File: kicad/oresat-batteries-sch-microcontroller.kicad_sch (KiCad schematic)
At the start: 31 parts, among them J4 ORESAT-DEBUG-CONNECTOR-ALL, U20 TCAN330, U21 STM32F091C, X3 ECS-160-10-36Q-ES-TR

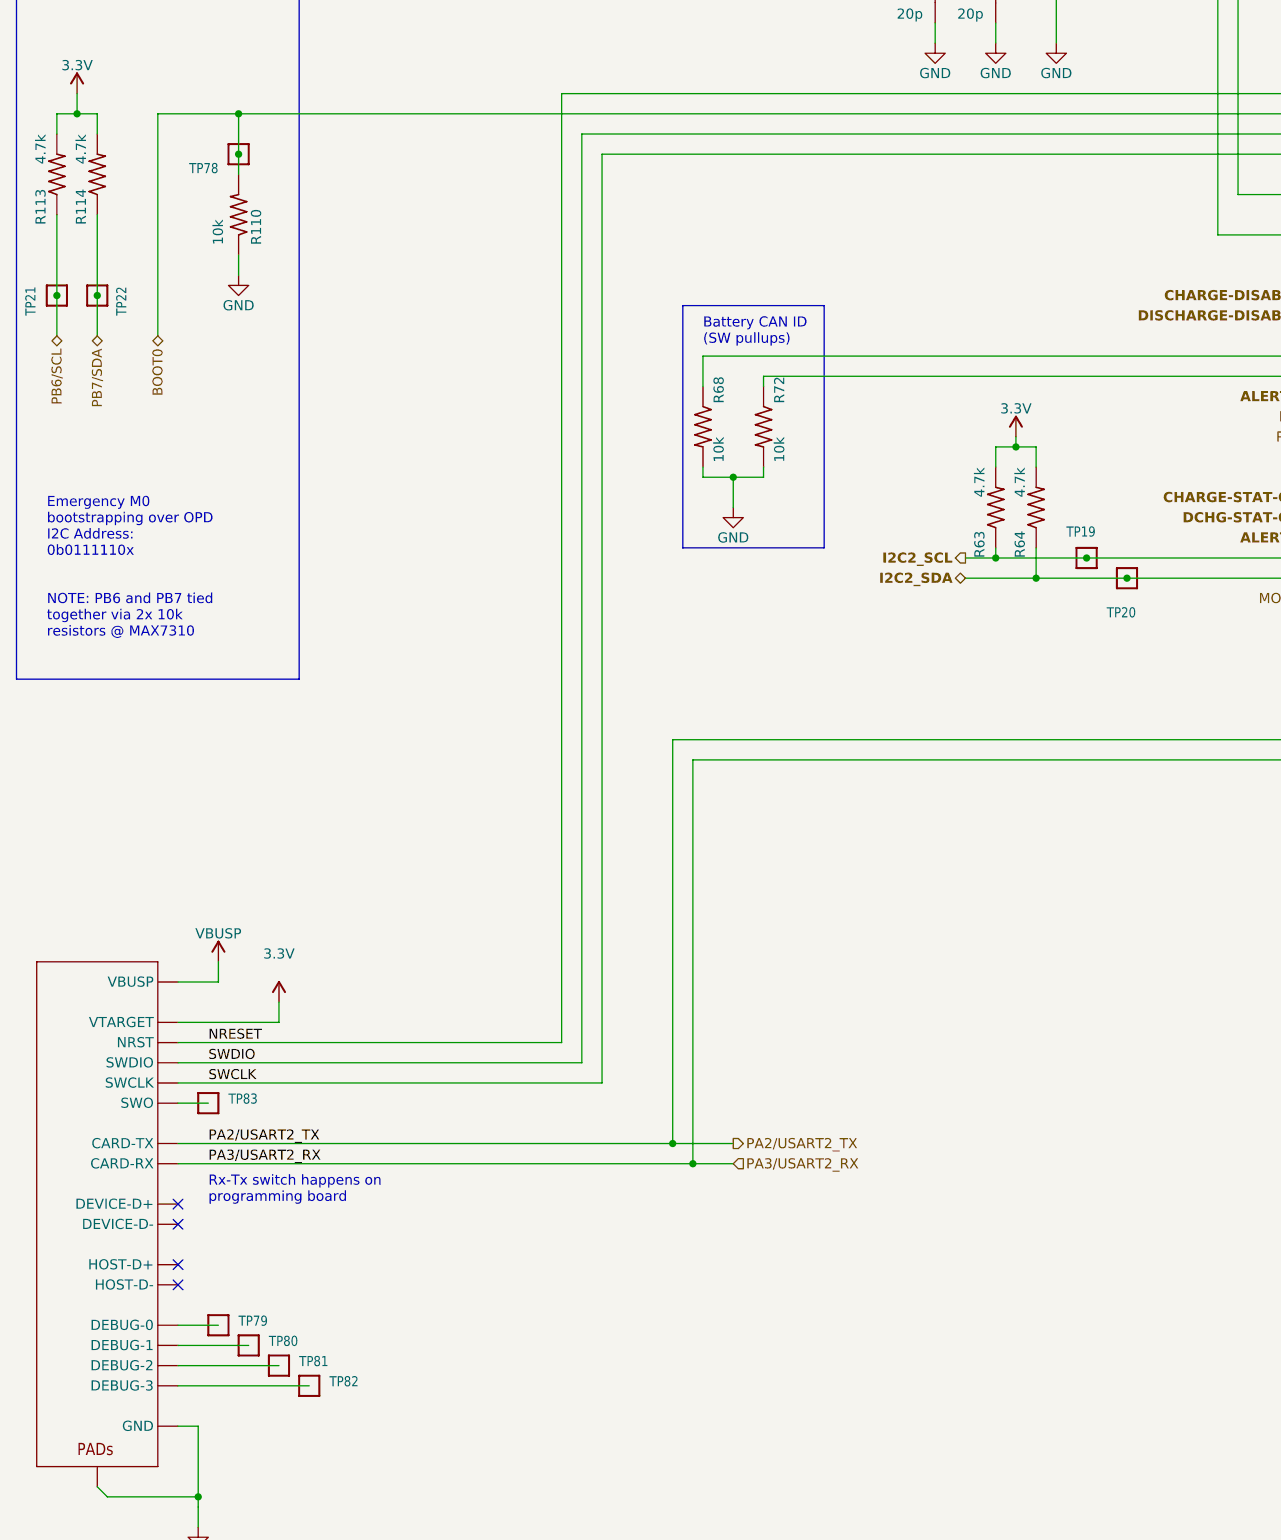
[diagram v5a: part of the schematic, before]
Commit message: Minor polishing, removing outdated OPD signals and OPD power jumper.
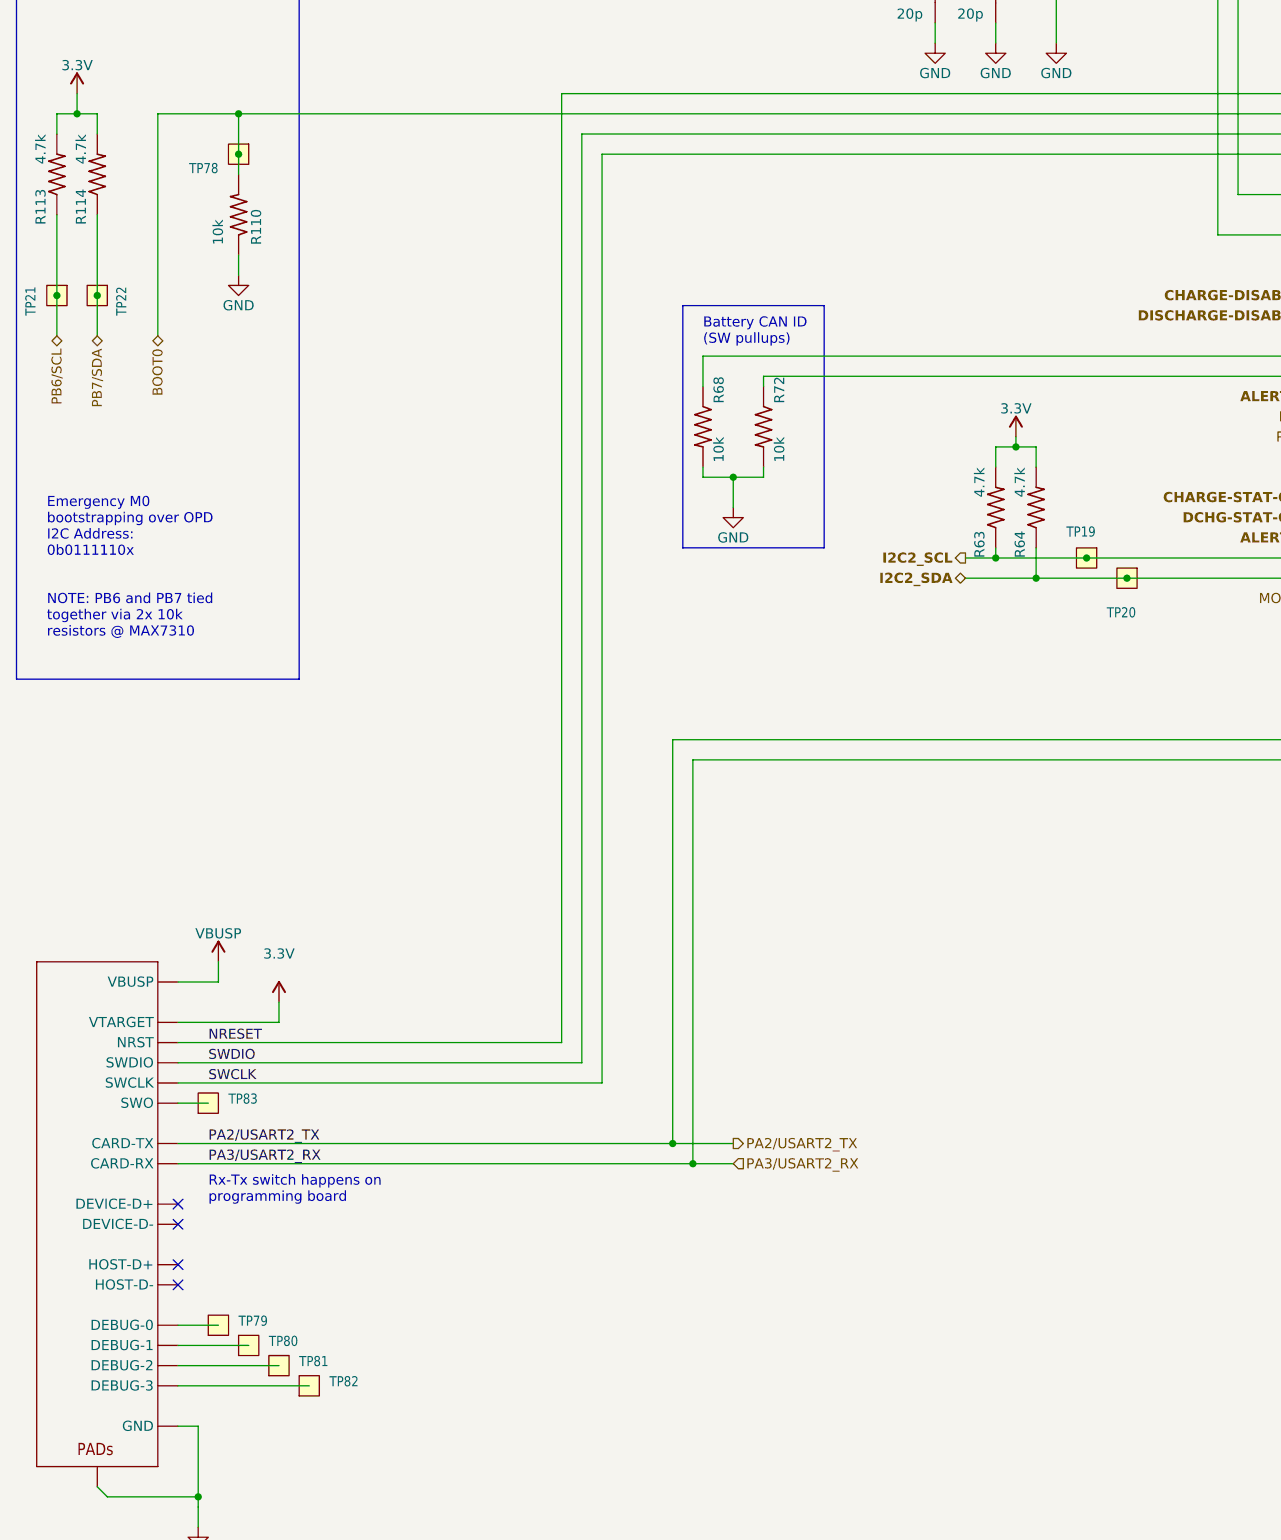
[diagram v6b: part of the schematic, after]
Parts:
- TP19, TP20, TP21, TP22, TP78, TP79, TP80, TP81, TP82, TP83: footprint oresat-batteries:1X01 -> oresat-misc:TestPoint-0.75mm-th; symbol oresat-batteries-eagle-import:TEST-POINT-LARGE-SQUARE -> oresat-misc:Test-Point-0.75mm-th; now left out of the parts list
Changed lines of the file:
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@@
 	)
 	(symbol
-		(lib_id "oresat-batteries-eagle-import:TEST-POINT-LARGE-SQUARE")
+		(lib_id "oresat-misc:Test-Point-0.75mm-th")
 		(at 52.07 213.36 0)
 		(mirror x)
 		(unit 1)
-		(exclude_from_sim no)
-		(in_bom yes)
+		(exclude_from_sim yes)
+		(in_bom no)
 		(on_board yes)
 		(dnp no)
@@
 			)
 		)
-		(property "Footprint" "oresat-batteries:1X01"
-			(at 52.07 213.36 0)
+		(property "Footprint" "oresat-misc:TestPoint-0.75mm-th"
+			(at 52.07 223.52 0)
 			(effects
 				(font
@@
 			)
 		)
-		(property "Description" ""
+		(property "Description" "0.75 mm TH test point; good for scope probes and jumpers"
 			(at 52.07 213.36 0)
 			(effects
@@
 					(size 1.27 1.27)
 				)
+				(hide yes)
 			)
 		)
@@
 	)
 	(symbol
-		(lib_id "oresat-batteries-eagle-import:TEST-POINT-LARGE-SQUARE")
+		(lib_id "oresat-misc:Test-Point-0.75mm-th")
 		(at 162.56 116.84 0)
 		(mirror y)
 		(unit 1)
-		(exclude_from_sim no)
-		(in_bom yes)
+		(exclude_from_sim yes)
+		(in_bom no)
 		(on_board yes)
 		(dnp no)
@@
 			)
 		)
-		(property "Footprint" "oresat-batteries:1X01"
-			(at 162.56 116.84 0)
+		(property "Footprint" "oresat-misc:TestPoint-0.75mm-th"
+			(at 162.56 106.68 0)
 			(effects
 				(font
@@
 			)
 		)
-		(property "Description" ""
+		(property "Description" "0.75 mm TH test point; good for scope probes and jumpers"
 			(at 162.56 116.84 0)
 			(effects
@@
 					(size 1.27 1.27)
 				)
+				(hide yes)
 			)
 		)
@@
 	)
 	(symbol
-		(lib_id "oresat-batteries-eagle-import:TEST-POINT-LARGE-SQUARE")
+		(lib_id "oresat-misc:Test-Point-0.75mm-th")
 		(at 27.94 81.28 0)
 		(mirror y)
 		(unit 1)
-		(exclude_from_sim no)
-		(in_bom yes)
+		(exclude_from_sim yes)
+		(in_bom no)
 		(on_board yes)
 		(dnp no)
@@
 			)
 		)
-		(property "Footprint" "oresat-batteries:1X01"
-			(at 27.94 81.28 0)
+		(property "Footprint" "oresat-misc:TestPoint-0.75mm-th"
+			(at 27.94 71.12 0)
 			(effects
 				(font
@@
 			)
 		)
-		(property "Description" ""
+		(property "Description" "0.75 mm TH test point; good for scope probes and jumpers"
 			(at 27.94 81.28 0)
 			(effects
@@
 					(size 1.27 1.27)
 				)
+				(hide yes)
 			)
 		)
@@
 	)
 	(symbol
-		(lib_id "oresat-batteries-eagle-import:TEST-POINT-LARGE-SQUARE")
+		(lib_id "oresat-misc:Test-Point-0.75mm-th")
 		(at 46.99 182.88 0)
 		(mirror x)
 		(unit 1)
-		(exclude_from_sim no)
-		(in_bom yes)
+		(exclude_from_sim yes)
+		(in_bom no)
 		(on_board yes)
 		(dnp no)
@@
 			)
 		)
-		(property "Footprint" "oresat-batteries:1X01"
-			(at 46.99 182.88 0)
+		(property "Footprint" "oresat-misc:TestPoint-0.75mm-th"
+			(at 46.99 193.04 0)
 			(effects
 				(font
@@
 			)
 		)
-		(property "Description" ""
+		(property "Description" "0.75 mm TH test point; good for scope probes and jumpers"
 			(at 46.99 182.88 0)
 			(effects
@@
 					(size 1.27 1.27)
 				)
+				(hide yes)
 			)
 		)
@@
 	)
 	(symbol
-		(lib_id "oresat-batteries-eagle-import:TEST-POINT-LARGE-SQUARE")
+		(lib_id "oresat-misc:Test-Point-0.75mm-th")
 		(at 59.69 218.44 0)
 		(mirror x)
 		(unit 1)
-		(exclude_from_sim no)
-		(in_bom yes)
+		(exclude_from_sim yes)
+		(in_bom no)
 		(on_board yes)
 		(dnp no)
@@
 			)
 		)
-		(property "Footprint" "oresat-batteries:1X01"
-			(at 59.69 218.44 0)
+		(property "Footprint" "oresat-misc:TestPoint-0.75mm-th"
+			(at 59.69 228.6 0)
 			(effects
 				(font
@@
 			)
 		)
-		(property "Description" ""
+		(property "Description" "0.75 mm TH test point; good for scope probes and jumpers"
 			(at 59.69 218.44 0)
 			(effects
@@
 					(size 1.27 1.27)
 				)
+				(hide yes)
 			)
 		)
@@
 	)
 	(symbol
-		(lib_id "oresat-batteries-eagle-import:TEST-POINT-LARGE-SQUARE")
+		(lib_id "oresat-misc:Test-Point-0.75mm-th")
 		(at 48.26 210.82 0)
 		(mirror x)
 		(unit 1)
-		(exclude_from_sim no)
-		(in_bom yes)
+		(exclude_from_sim yes)
+		(in_bom no)
 		(on_board yes)
 		(dnp no)
@@
 			)
 		)
-		(property "Footprint" "oresat-batteries:1X01"
-			(at 48.26 210.82 0)
+		(property "Footprint" "oresat-misc:TestPoint-0.75mm-th"
+			(at 48.26 220.98 0)
 			(effects
 				(font
@@
 			)
 		)
-		(property "Description" ""
+		(property "Description" "0.75 mm TH test point; good for scope probes and jumpers"
 			(at 48.26 210.82 0)
 			(effects
@@
 					(size 1.27 1.27)
 				)
+				(hide yes)
 			)
 		)
@@
 	)
 	(symbol
-		(lib_id "oresat-batteries-eagle-import:TEST-POINT-LARGE-SQUARE")
+		(lib_id "oresat-misc:Test-Point-0.75mm-th")
 		(at 55.88 215.9 0)
 		(mirror x)
 		(unit 1)
-		(exclude_from_sim no)
-		(in_bom yes)
+		(exclude_from_sim yes)
+		(in_bom no)
 		(on_board yes)
 		(dnp no)
@@
 			)
 		)
-		(property "Footprint" "oresat-batteries:1X01"
-			(at 55.88 215.9 0)
+		(property "Footprint" "oresat-misc:TestPoint-0.75mm-th"
+			(at 55.88 226.06 0)
 			(effects
 				(font
@@
 			)
 		)
-		(property "Description" ""
+		(property "Description" "0.75 mm TH test point; good for scope probes and jumpers"
 			(at 55.88 215.9 0)
 			(effects
@@
 					(size 1.27 1.27)
 				)
+				(hide yes)
 			)
 		)
@@
 	)
 	(symbol
-		(lib_id "oresat-batteries-eagle-import:TEST-POINT-LARGE-SQUARE")
+		(lib_id "oresat-misc:Test-Point-0.75mm-th")
 		(at 157.48 114.3 0)
 		(mirror y)
 		(unit 1)
-		(exclude_from_sim no)
-		(in_bom yes)
+		(exclude_from_sim yes)
+		(in_bom no)
 		(on_board yes)
 		(dnp no)
@@
 			)
 		)
-		(property "Footprint" "oresat-batteries:1X01"
-			(at 157.48 114.3 0)
+		(property "Footprint" "oresat-misc:TestPoint-0.75mm-th"
+			(at 157.48 104.14 0)
 			(effects
 				(font
@@
 			)
 		)
-		(property "Description" ""
+		(property "Description" "0.75 mm TH test point; good for scope probes and jumpers"
 			(at 157.48 114.3 0)
 			(effects
@@
 					(size 1.27 1.27)
 				)
+				(hide yes)
 			)
 		)
@@
 	)
 	(symbol
-		(lib_id "oresat-batteries-eagle-import:TEST-POINT-LARGE-SQUARE")
+		(lib_id "oresat-misc:Test-Point-0.75mm-th")
 		(at 33.02 81.28 0)
 		(mirror y)
 		(unit 1)
-		(exclude_from_sim no)
-		(in_bom yes)
+		(exclude_from_sim yes)
+		(in_bom no)
 		(on_board yes)
 		(dnp no)
@@
 			)
 		)
-		(property "Footprint" "oresat-batteries:1X01"
-			(at 33.02 81.28 0)
+		(property "Footprint" "oresat-misc:TestPoint-0.75mm-th"
+			(at 33.02 71.12 0)
 			(effects
 				(font
@@
 			)
 		)
-		(property "Description" ""
+		(property "Description" "0.75 mm TH test point; good for scope probes and jumpers"
 			(at 33.02 81.28 0)
 			(effects
@@
 					(size 1.27 1.27)
 				)
+				(hide yes)
 			)
 		)
@@
 	)
 	(symbol
-		(lib_id "oresat-batteries-eagle-import:TEST-POINT-LARGE-SQUARE")
+		(lib_id "oresat-misc:Test-Point-0.75mm-th")
 		(at 50.8 63.5 0)
 		(mirror y)
 		(unit 1)
-		(exclude_from_sim no)
-		(in_bom yes)
+		(exclude_from_sim yes)
+		(in_bom no)
 		(on_board yes)
 		(dnp no)
@@
 			)
 		)
-		(property "Footprint" "oresat-batteries:1X01"
-			(at 50.8 63.5 0)
+		(property "Footprint" "oresat-misc:TestPoint-0.75mm-th"
+			(at 50.8 53.34 0)
 			(effects
 				(font
@@
 			)
 		)
-		(property "Description" ""
+		(property "Description" "0.75 mm TH test point; good for scope probes and jumpers"
 			(at 50.8 63.5 0)
 			(effects
@@
 					(size 1.27 1.27)
 				)
+				(hide yes)
 			)
 		)

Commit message: Renovated Schematic
Updated schematic symbols and made more uniform with changed resistor, capacitor, and FET symbols. Changed 0603 cap foot print to 0603 small in Oresat passives. Added 2 new resistors and 2 new caps in the power page. Removed old debug connector in favor of the new one. The changes made should make very little updates when pushing the changes to the PCB.
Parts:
- removed J4: ORESAT-DEBUG-CONNECTOR-ALL, oresat-batteries:TE_2-1734592-0, symbol oresat-batteries-eagle-import:ORESAT-DEBUG-CONNECTOR-ALL
- removed TP79, TP80, TP81, TP82: TEST-POINT-LARGE-SQUARE, oresat-misc:TestPoint-0.75mm-th, symbol oresat-misc:Test-Point-0.75mm-th
- added J2: SM14B-SHLS-TF, oresat-connectors:J-JST-SM14BSHLSTF, symbol oresat-connectors:ORESAT-DEBUG-CONNECTOR-3
- added TP34: TEST-POINT-LARGE-SQUARE, oresat-misc:TestPoint-0.75mm-th, symbol oresat-misc:Test-Point-0.75mm-th
- C44, C45, C46, C47, C48, C49, C50: footprint oresat-batteries:.0603-C-NOSILK -> oresat-passives:c_0603-SMALL; symbol oresat-batteries-eagle-import:C-EU0603-C-NOSILK -> Device:C_Small
- R110, R111, R112, R113, R114, R63, R64, R68, R72: symbol oresat-batteries-eagle-import:R-US_0603-C-NOSILK -> Device:R_Small_US
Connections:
- net 3.3V: now also J2.9 (VTARGET)
- net BOOT0: now also R110.1; no longer R110.2
- net GND: now also R110.2, J2.14 (GND), J2.15 (PAD), J2.16 (PAD), J2.5 (GND); no longer R110.1
- net NRESET: now also J2.10 (NRST)
- net PA2/USART2_TX: now also J2.6 (CARD-TX)
- net PA3/USART2_RX: now also J2.7 (CARD-RX)
- net SWCLK: now also J2.12 (SWCLK)
- net SWDIO: now also J2.11 (SWDIO)
- net VBUSP: now also J2.1 (VBUSP), J2.2 (VBUSP)
- net at TP83.1: now also J2.13 (SWO)
- new net: J2.8 (DEBUG-0), TP34.1
- no-connect marks 10 -> 8
